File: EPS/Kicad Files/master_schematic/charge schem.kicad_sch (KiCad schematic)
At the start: 23 parts, among them J1 USB_C_Receptacle, U1 MAX77757JEFG435+, U2 MAX17055EWL+T

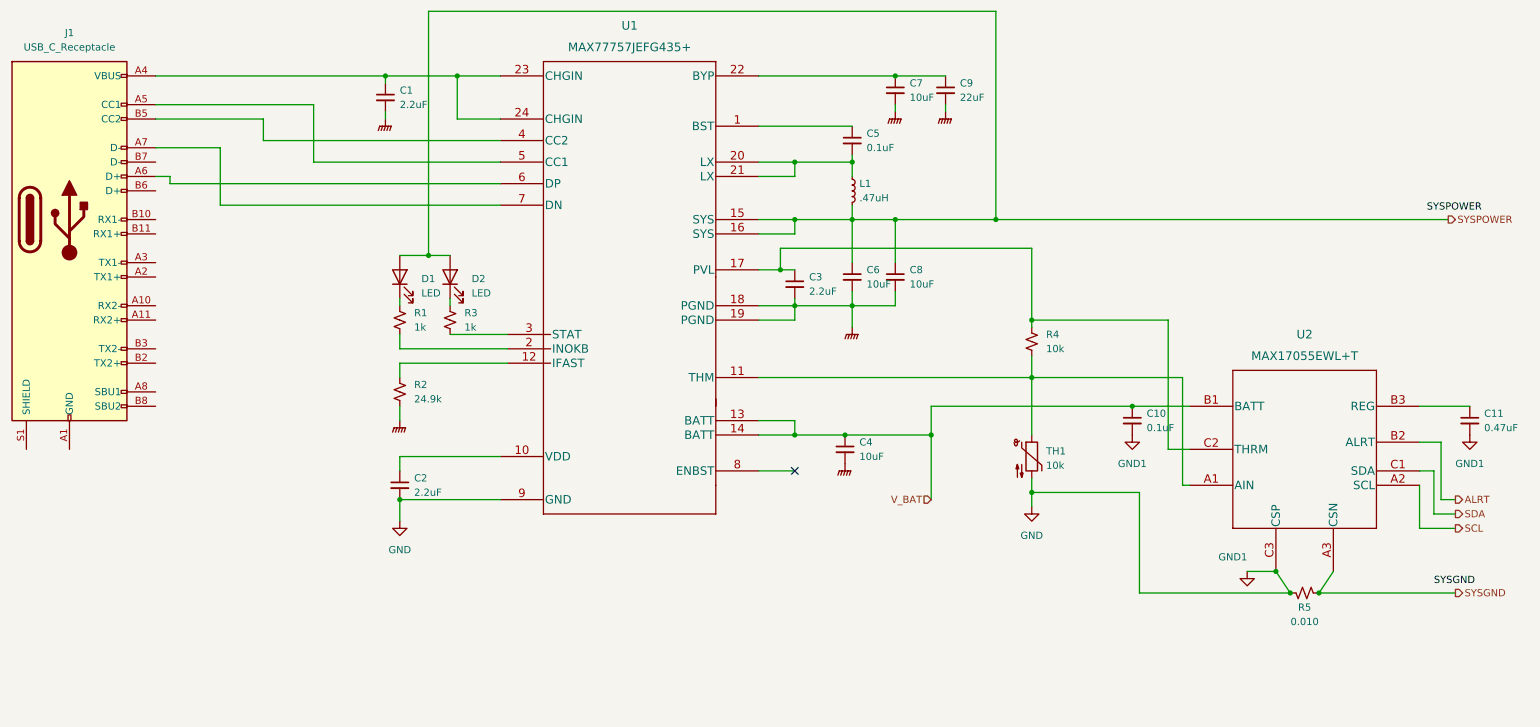
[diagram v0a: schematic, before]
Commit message: revised EPS schematics
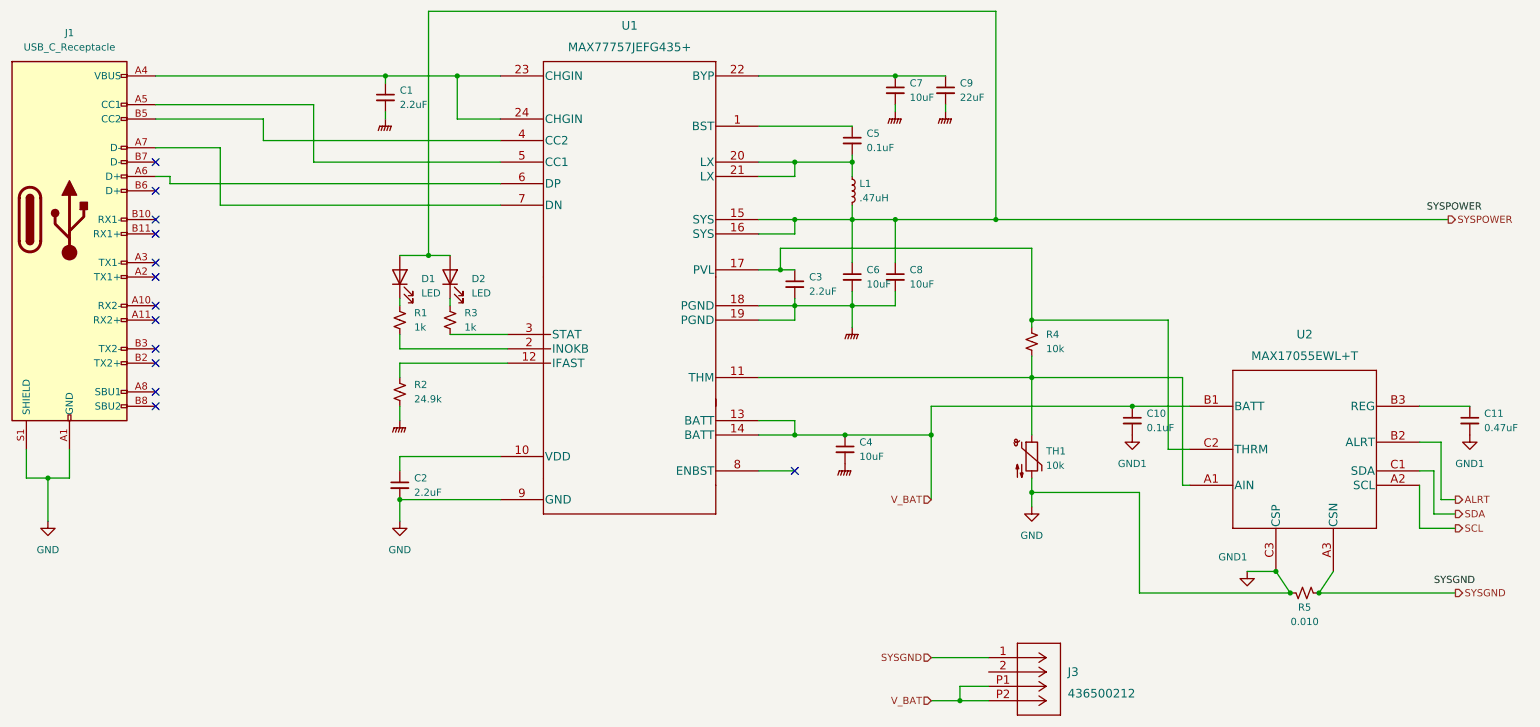
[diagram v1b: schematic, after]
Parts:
- added J3: 436500212, molex connector:436500212, symbol molex connector:436500212
- U1: footprint 77757 foot:IC_MAX77757JEFG435+ -> max77757:IC_MAX77757JEFG435+
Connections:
- net GND: now also J1.A1 (GND), J1.A12 (GND), J1.B1 (GND), J1.B12 (GND), J1.S1 (SHIELD)
- net SYSGND: now also J3.1
- net V_BAT: now also J3.P1, J3.P2
- no-connect marks 1 -> 13
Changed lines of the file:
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@@
     (title "Charge Circuit")
   )
+  (junction (at 26.67 106.68) (diameter 0) (color 0 0 0 0)
+  )
   (junction (at 246.38 127) (diameter 0) (color 0 0 0 0)
   )
@@
   (junction (at 200.66 78.74) (diameter 0) (color 0 0 0 0)
   )
+  (junction (at 187.96 146.05) (diameter 0) (color 0 0 0 0)
+  )
   (junction (at 168.91 50.8) (diameter 0) (color 0 0 0 0)
   )
@@
   )
   (no_connect (at 158.75 105.41))
+  (no_connect (at 45.72 50.8))
+  (no_connect (at 45.72 55.88))
+  (no_connect (at 45.72 60.96))
+  (no_connect (at 45.72 63.5))
+  (no_connect (at 45.72 68.58))
+  (no_connect (at 45.72 86.36))
+  (no_connect (at 45.72 91.44))
+  (no_connect (at 45.72 93.98))
+  (no_connect (at 45.72 71.12))
+  (no_connect (at 45.72 76.2))
+  (no_connect (at 45.72 78.74))
+  (no_connect (at 45.72 83.82))
   (wire (pts (xy 182.88 93.98) (xy 182.88 99.06))
     (stroke (width 0) (type default) (color 0 0 0 0))
@@
     (stroke (width 0) (type default) (color 0 0 0 0))
   )
+  (wire (pts (xy 187.96 146.05) (xy 193.04 146.05))
+    (stroke (width 0) (type default) (color 0 0 0 0))
+  )
   (wire (pts (xy 168.91 80.01) (xy 168.91 76.2))
     (stroke (width 0) (type default) (color 0 0 0 0))
@@
     (stroke (width 0) (type default) (color 0 0 0 0))
   )
+  (wire (pts (xy 182.88 146.05) (xy 187.96 146.05))
+    (stroke (width 0) (type default) (color 0 0 0 0))
+  )
   (wire (pts (xy 158.75 53.34) (xy 158.75 50.8))
     (stroke (width 0) (type default) (color 0 0 0 0))
@@
     (stroke (width 0) (type default) (color 0 0 0 0))
   )
+  (wire (pts (xy 187.96 143.51) (xy 187.96 146.05))
+    (stroke (width 0) (type default) (color 0 0 0 0))
+  )
   (wire (pts (xy 200.66 109.22) (xy 219.71 109.22))
     (stroke (width 0) (type default) (color 0 0 0 0))
@@
     (stroke (width 0) (type default) (color 0 0 0 0))
   )
+  (wire (pts (xy 193.04 138.43) (xy 182.88 138.43))
+    (stroke (width 0) (type default) (color 0 0 0 0))
+  )
   (wire (pts (xy 158.75 96.52) (xy 158.75 99.06))
     (stroke (width 0) (type default) (color 0 0 0 0))
@@
     (stroke (width 0) (type default) (color 0 0 0 0))
   )
+  (wire (pts (xy 26.67 106.68) (xy 30.48 106.68))
+    (stroke (width 0) (type default) (color 0 0 0 0))
+  )
   (wire (pts (xy 269.24 107.95) (xy 269.24 115.57))
     (stroke (width 0) (type default) (color 0 0 0 0))
@@
     (stroke (width 0) (type default) (color 0 0 0 0))
   )
+  (wire (pts (xy 193.04 143.51) (xy 187.96 143.51))
+    (stroke (width 0) (type default) (color 0 0 0 0))
+  )
   (wire (pts (xy 107.95 83.82) (xy 88.9 83.82))
     (stroke (width 0) (type default) (color 0 0 0 0))
@@
     (stroke (width 0) (type default) (color 0 0 0 0))
   )
+  (wire (pts (xy 26.67 114.3) (xy 26.67 106.68))
+    (stroke (width 0) (type default) (color 0 0 0 0))
+  )
   (wire (pts (xy 45.72 35.56) (xy 86.36 35.56))
     (stroke (width 0) (type default) (color 0 0 0 0))
@@
     (stroke (width 0) (type default) (color 0 0 0 0))
   )
+  (wire (pts (xy 30.48 106.68) (xy 30.48 101.6))
+    (stroke (width 0) (type default) (color 0 0 0 0))
+  )
   (wire (pts (xy 93.98 24.13) (xy 93.98 67.31))
     (stroke (width 0) (type default) (color 0 0 0 0))
@@
     (stroke (width 0) (type default) (color 0 0 0 0))
   )
+  (wire (pts (xy 22.86 101.6) (xy 22.86 106.68))
+    (stroke (width 0) (type default) (color 0 0 0 0))
+  )
   (wire (pts (xy 86.36 41.91) (xy 86.36 43.18))
     (stroke (width 0) (type default) (color 0 0 0 0))
@@
   )
   (wire (pts (xy 86.36 35.56) (xy 99.06 35.56))
+    (stroke (width 0) (type default) (color 0 0 0 0))
+  )
+  (wire (pts (xy 22.86 106.68) (xy 26.67 106.68))
     (stroke (width 0) (type default) (color 0 0 0 0))
   )
@@
     (effects (font (size 1.27 1.27)) (justify left bottom))
   )
+  (hierarchical_label "V_BAT" (shape input) (at 182.88 146.05 180)
+    (effects (font (size 1.27 1.27)) (justify right))
+  )
   (hierarchical_label "SYSPOWER" (shape output) (at 274.32 60.96 0)
     (effects (font (size 1.27 1.27)) (justify left))
@@
   (hierarchical_label "SYSGND" (shape output) (at 275.59 127 0)
     (effects (font (size 1.27 1.27)) (justify left))
+  )
+  (hierarchical_label "SYSGND" (shape input) (at 182.88 138.43 180)
+    (effects (font (size 1.27 1.27)) (justify right))
   )
   (hierarchical_label "SCL" (shape output) (at 275.59 115.57 0)
@@
     (pin "1")
     (pin "2")
+  )
+  (symbol (lib_id "molex connector:436500212") (at 193.04 138.43 0) (unit 1)
+    (in_bom yes) (on_board yes) (fields_autoplaced)
+    (property "Reference" "J3" (id 0) (at 207.01 140.97 0)
+      (effects (font (size 1.524 1.524)) (justify left))
+    )
+    (property "Value" "436500212" (id 1) (at 207.01 144.78 0)
+      (effects (font (size 1.524 1.524)) (justify left))
+    )
+    (property "Footprint" "molex connector:436500212" (id 2) (at 203.2 145.034 0)
+      (effects (font (size 1.524 1.524)) hide)
+    )
+    (property "Datasheet" "" (id 3) (at 193.04 138.43 0)
+      (effects (font (size 1.524 1.524)))
+    )
+    (pin "1")
+    (pin "2")
+    (pin "P1")
+    (pin "P2")
   )
   (symbol (lib_id "Device:C_Small") (at 218.44 96.52 0) (unit 1)
@@
       (effects (font (size 1.524 1.524)))
     )
-    (property "Footprint" "77757 foot:IC_MAX77757JEFG435+" (id 2) (at 129.54 32.004 0)
+    (property "Footprint" "max77757:IC_MAX77757JEFG435+" (id 2) (at 129.54 32.004 0)
       (effects (font (size 1.524 1.524)) hide)
     )
@@
     (pin "9")
   )
+  (symbol (lib_id "power:GND") (at 26.67 114.3 0) (unit 1)
+    (in_bom yes) (on_board yes) (fields_autoplaced)
+    (property "Reference" "#PWR0121" (id 0) (at 26.67 120.65 0)
+      (effects (font (size 1.27 1.27)) hide)
+    )
+    (property "Value" "GND" (id 1) (at 26.67 119.38 0))
+    (property "Footprint" "" (id 2) (at 26.67 114.3 0)
+      (effects (font (size 1.27 1.27)) hide)
+    )
+    (property "Datasheet" "" (id 3) (at 26.67 114.3 0)
+      (effects (font (size 1.27 1.27)) hide)
+    )
+    (pin "1")
+  )
   (symbol (lib_id "Device:C_Small") (at 176.53 71.12 0) (unit 1)

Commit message: updated master schematic
should be nearing final schematic revision. run electrical rules check next
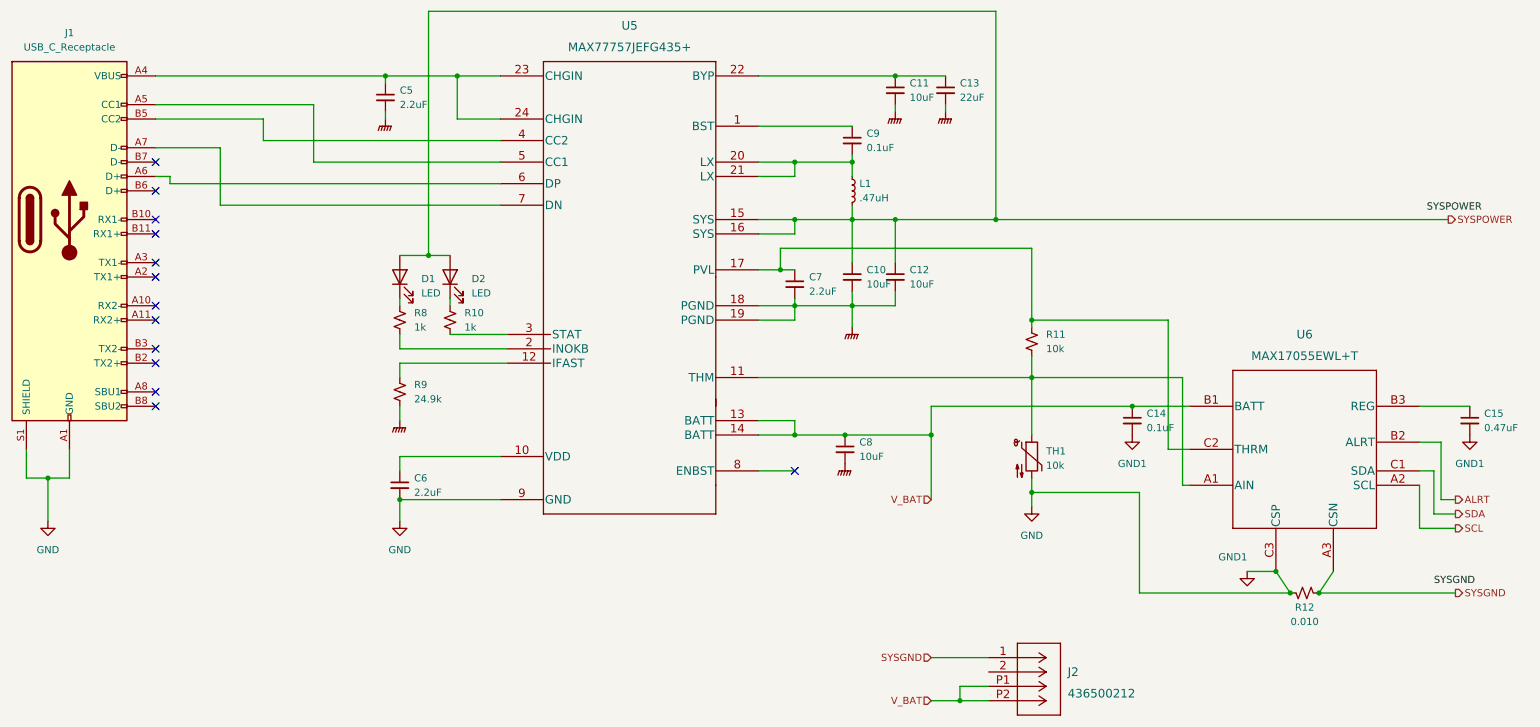
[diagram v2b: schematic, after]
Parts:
- renumbered C6 to C10, C7 to C11, C8 to C12, C9 to C13, C10 to C14, C11 to C15, C1 to C5, C2 to C6, C3 to C7, C4 to C8, C5 to C9, J3 to J2, R3 to R10, R4 to R11, R5 to R12, R1 to R8, R2 to R9, U1 to U5, U2 to U6
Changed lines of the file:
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@@
   (symbol (lib_id "power:GNDPWR") (at 86.36 43.18 0) (unit 1)
     (in_bom yes) (on_board yes) (fields_autoplaced)
-    (property "Reference" "#PWR0106" (id 0) (at 86.36 48.26 0)
+    (property "Reference" "#PWR012" (id 0) (at 86.36 48.26 0)
       (effects (font (size 1.27 1.27)) hide)
     )
@@
   (symbol (lib_id "power:GNDPWR") (at 168.91 80.01 0) (unit 1)
     (in_bom yes) (on_board yes) (fields_autoplaced)
-    (property "Reference" "#PWR0108" (id 0) (at 168.91 85.09 0)
+    (property "Reference" "#PWR016" (id 0) (at 168.91 85.09 0)
       (effects (font (size 1.27 1.27)) hide)
     )
@@
   (symbol (lib_id "Device:R_Small_US") (at 248.92 127 90) (mirror x) (unit 1)
     (in_bom yes) (on_board yes)
-    (property "Reference" "R5" (id 0) (at 248.92 129.54 90))
+    (property "Reference" "R12" (id 0) (at 248.92 129.54 90))
     (property "Value" "0.010" (id 1) (at 248.92 132.08 90))
     (property "Footprint" "Resistor_SMD:R_0805_2012Metric" (id 2) (at 248.92 127 0)
@@
   (symbol (lib_id "Device:C_Small") (at 185.42 38.1 0) (unit 1)
     (in_bom yes) (on_board yes) (fields_autoplaced)
-    (property "Reference" "C9" (id 0) (at 187.96 36.8362 0)
+    (property "Reference" "C13" (id 0) (at 187.96 36.8362 0)
       (effects (font (size 1.27 1.27)) (justify left))
     )
@@
   (symbol (lib_id "Device:C_Small") (at 88.9 107.95 0) (unit 1)
     (in_bom yes) (on_board yes) (fields_autoplaced)
-    (property "Reference" "C2" (id 0) (at 91.44 106.6862 0)
+    (property "Reference" "C6" (id 0) (at 91.44 106.6862 0)
       (effects (font (size 1.27 1.27)) (justify left))
     )
@@
   (symbol (lib_id "molex connector:436500212") (at 193.04 138.43 0) (unit 1)
     (in_bom yes) (on_board yes) (fields_autoplaced)
-    (property "Reference" "J3" (id 0) (at 207.01 140.97 0)
+    (property "Reference" "J2" (id 0) (at 207.01 140.97 0)
       (effects (font (size 1.524 1.524)) (justify left))
     )
@@
   (symbol (lib_id "Device:C_Small") (at 218.44 96.52 0) (unit 1)
     (in_bom yes) (on_board yes) (fields_autoplaced)
-    (property "Reference" "C10" (id 0) (at 220.98 95.2562 0)
+    (property "Reference" "C14" (id 0) (at 220.98 95.2562 0)
       (effects (font (size 1.27 1.27)) (justify left))
     )
@@
   (symbol (lib_id "power:GND1") (at 218.44 99.06 0) (unit 1)
     (in_bom yes) (on_board yes) (fields_autoplaced)
-    (property "Reference" "#PWR0109" (id 0) (at 218.44 105.41 0)
+    (property "Reference" "#PWR020" (id 0) (at 218.44 105.41 0)
       (effects (font (size 1.27 1.27)) hide)
     )
@@
   (symbol (lib_id "power:GND") (at 88.9 114.3 0) (unit 1)
     (in_bom yes) (on_board yes) (fields_autoplaced)
-    (property "Reference" "#PWR0101" (id 0) (at 88.9 120.65 0)
+    (property "Reference" "#PWR014" (id 0) (at 88.9 120.65 0)
       (effects (font (size 1.27 1.27)) hide)
     )
@@
   (symbol (lib_id "power:GNDPWR") (at 185.42 41.91 0) (unit 1)
     (in_bom yes) (on_board yes) (fields_autoplaced)
-    (property "Reference" "#PWR01" (id 0) (at 185.42 46.99 0)
+    (property "Reference" "#PWR018" (id 0) (at 185.42 46.99 0)
       (effects (font (size 1.27 1.27)) hide)
     )
@@
   (symbol (lib_id "Device:C_Small") (at 278.13 96.52 0) (unit 1)
     (in_bom yes) (on_board yes) (fields_autoplaced)
-    (property "Reference" "C11" (id 0) (at 280.67 95.2562 0)
+    (property "Reference" "C15" (id 0) (at 280.67 95.2562 0)
       (effects (font (size 1.27 1.27)) (justify left))
     )
@@
   (symbol (lib_id "Device:C_Small") (at 158.75 72.39 0) (unit 1)
     (in_bom yes) (on_board yes) (fields_autoplaced)
-    (property "Reference" "C3" (id 0) (at 161.29 71.1262 0)
+    (property "Reference" "C7" (id 0) (at 161.29 71.1262 0)
       (effects (font (size 1.27 1.27)) (justify left))
     )
@@
   (symbol (lib_name "MAX17055EWL+T_1") (lib_id "MAX17055:MAX17055EWL+T") (at 228.6 92.71 0) (unit 1)
     (in_bom yes) (on_board yes) (fields_autoplaced)
-    (property "Reference" "U2" (id 0) (at 248.92 81.28 0)
+    (property "Reference" "U6" (id 0) (at 248.92 81.28 0)
       (effects (font (size 1.524 1.524)))
     )
@@
   (symbol (lib_id "power:GND1") (at 278.13 99.06 0) (unit 1)
     (in_bom yes) (on_board yes) (fields_autoplaced)
-    (property "Reference" "#PWR0110" (id 0) (at 278.13 105.41 0)
+    (property "Reference" "#PWR022" (id 0) (at 278.13 105.41 0)
       (effects (font (size 1.27 1.27)) hide)
     )
@@
   (symbol (lib_id "Device:R_Small_US") (at 88.9 78.74 0) (unit 1)
     (in_bom yes) (on_board yes) (fields_autoplaced)
-    (property "Reference" "R1" (id 0) (at 91.44 77.4699 0)
+    (property "Reference" "R8" (id 0) (at 91.44 77.4699 0)
       (effects (font (size 1.27 1.27)) (justify left))
     )
@@
   (symbol (lib_id "Device:C_Small") (at 176.53 38.1 0) (unit 1)
     (in_bom yes) (on_board yes) (fields_autoplaced)
-    (property "Reference" "C7" (id 0) (at 179.07 36.8362 0)
+    (property "Reference" "C11" (id 0) (at 179.07 36.8362 0)
       (effects (font (size 1.27 1.27)) (justify left))
     )
@@
   (symbol (lib_id "Device:R_Small_US") (at 88.9 91.44 0) (unit 1)
     (in_bom yes) (on_board yes) (fields_autoplaced)
-    (property "Reference" "R2" (id 0) (at 91.44 90.1699 0)
+    (property "Reference" "R9" (id 0) (at 91.44 90.1699 0)
       (effects (font (size 1.27 1.27)) (justify left))
     )
@@
   (symbol (lib_id "Device:R_Small_US") (at 97.79 78.74 0) (unit 1)
     (in_bom yes) (on_board yes) (fields_autoplaced)
-    (property "Reference" "R3" (id 0) (at 100.33 77.4699 0)
+    (property "Reference" "R10" (id 0) (at 100.33 77.4699 0)
       (effects (font (size 1.27 1.27)) (justify left))
     )
@@
   (symbol (lib_id "power:GNDPWR") (at 88.9 96.52 0) (unit 1)
     (in_bom yes) (on_board yes) (fields_autoplaced)
-    (property "Reference" "#PWR0105" (id 0) (at 88.9 101.6 0)
+    (property "Reference" "#PWR013" (id 0) (at 88.9 101.6 0)
       (effects (font (size 1.27 1.27)) hide)
     )
@@
   (symbol (lib_id "Device:R_Small_US") (at 200.66 82.55 0) (unit 1)
     (in_bom yes) (on_board yes) (fields_autoplaced)
-    (property "Reference" "R4" (id 0) (at 203.2 81.2799 0)
+    (property "Reference" "R11" (id 0) (at 203.2 81.2799 0)
       (effects (font (size 1.27 1.27)) (justify left))
     )
@@
   (symbol (lib_id "power:GNDPWR") (at 176.53 41.91 0) (unit 1)
     (in_bom yes) (on_board yes) (fields_autoplaced)
-    (property "Reference" "#PWR0102" (id 0) (at 176.53 46.99 0)
+    (property "Reference" "#PWR017" (id 0) (at 176.53 46.99 0)
       (effects (font (size 1.27 1.27)) hide)
     )
@@
   (symbol (lib_id "Device:C_Small") (at 168.91 46.99 0) (unit 1)
     (in_bom yes) (on_board yes) (fields_autoplaced)
-    (property "Reference" "C5" (id 0) (at 171.45 45.7262 0)
+    (property "Reference" "C9" (id 0) (at 171.45 45.7262 0)
       (effects (font (size 1.27 1.27)) (justify left))
     )
@@
   (symbol (lib_id "MAX77757_functional:MAX77757JEFG435+") (at 106.68 38.1 0) (unit 1)
     (in_bom yes) (on_board yes) (fields_autoplaced)
-    (property "Reference" "U1" (id 0) (at 129.54 26.67 0)
+    (property "Reference" "U5" (id 0) (at 129.54 26.67 0)
       (effects (font (size 1.524 1.524)))
     )
@@
   (symbol (lib_id "power:GND") (at 26.67 114.3 0) (unit 1)
     (in_bom yes) (on_board yes) (fields_autoplaced)
-    (property "Reference" "#PWR0121" (id 0) (at 26.67 120.65 0)
+    (property "Reference" "#PWR011" (id 0) (at 26.67 120.65 0)
       (effects (font (size 1.27 1.27)) hide)
     )
@@
   (symbol (lib_id "Device:C_Small") (at 176.53 71.12 0) (unit 1)
     (in_bom yes) (on_board yes) (fields_autoplaced)
-    (property "Reference" "C8" (id 0) (at 179.07 69.8562 0)
+    (property "Reference" "C12" (id 0) (at 179.07 69.8562 0)
       (effects (font (size 1.27 1.27)) (justify left))
     )
@@
   (symbol (lib_id "Device:C_Small") (at 86.36 39.37 0) (unit 1)
     (in_bom yes) (on_board yes) (fields_autoplaced)
-    (property "Reference" "C1" (id 0) (at 88.9 38.1062 0)
+    (property "Reference" "C5" (id 0) (at 88.9 38.1062 0)
       (effects (font (size 1.27 1.27)) (justify left))
     )
@@
   (symbol (lib_id "power:GND1") (at 238.76 123.19 0) (unit 1)
     (in_bom yes) (on_board yes)
-    (property "Reference" "#PWR0111" (id 0) (at 238.76 129.54 0)
+    (property "Reference" "#PWR021" (id 0) (at 238.76 129.54 0)
       (effects (font (size 1.27 1.27)) hide)
     )
@@
   (symbol (lib_id "power:GNDPWR") (at 167.64 104.14 0) (unit 1)
     (in_bom yes) (on_board yes) (fields_autoplaced)
-    (property "Reference" "#PWR0107" (id 0) (at 167.64 109.22 0)
+    (property "Reference" "#PWR015" (id 0) (at 167.64 109.22 0)
       (effects (font (size 1.27 1.27)) hide)
     )
@@
   (symbol (lib_id "Device:C_Small") (at 167.64 101.6 0) (unit 1)
     (in_bom yes) (on_board yes) (fields_autoplaced)
-    (property "Reference" "C4" (id 0) (at 170.18 100.3362 0)
+    (property "Reference" "C8" (id 0) (at 170.18 100.3362 0)
       (effects (font (size 1.27 1.27)) (justify left))
     )
@@
   (symbol (lib_id "Device:C_Small") (at 168.91 71.12 0) (unit 1)
     (in_bom yes) (on_board yes) (fields_autoplaced)
-    (property "Reference" "C6" (id 0) (at 171.45 69.8562 0)
+    (property "Reference" "C10" (id 0) (at 171.45 69.8562 0)
       (effects (font (size 1.27 1.27)) (justify left))
     )
@@
   (symbol (lib_id "power:GND") (at 200.66 111.76 0) (unit 1)
     (in_bom yes) (on_board yes) (fields_autoplaced)
-    (property "Reference" "#PWR0104" (id 0) (at 200.66 118.11 0)
-      (effects (font (size 1.27 1.27)) hide)
-    )
+    (property "Reference" "#PWR019" (id 0) (at 200.66 118.11 0)
+      (effects (font (size 1.27 1.27)) hide)
+    )
